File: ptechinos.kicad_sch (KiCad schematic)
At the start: 58 parts, among them J1 Bat_Pos, J2 Battery, J3 Bat_GND, J4 AudioJack4, SW1 SW_Power, SW2 Reset, U1 ProMicro

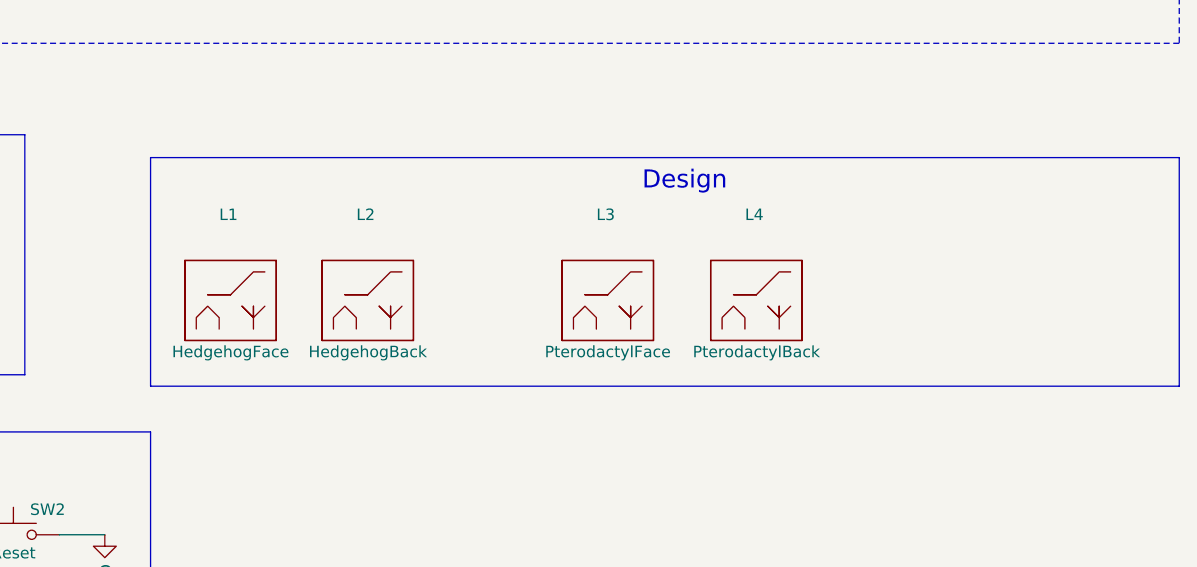
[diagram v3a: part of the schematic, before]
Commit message: ♻️ - Update PCB and schema with new drawing / board name. Update project date to today.
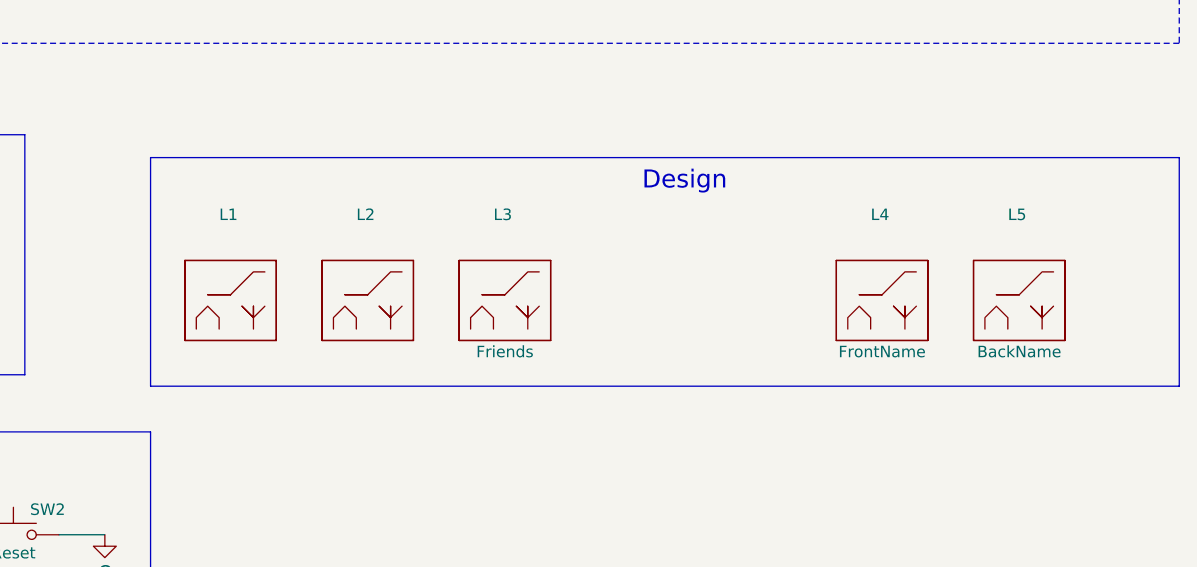
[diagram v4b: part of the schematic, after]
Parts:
- added L5: BackName, ptechinos:Board_name, symbol ptechinos:Logo
- L1: value HedgehogFace -> (none); footprint ptechinos:hedgehog-medium -> (none)
- L2: value HedgehogBack -> (none); footprint ptechinos:hedgehog-medium -> (none)
- L3: value PterodactylFace -> Friends; footprint ptechinos:pterodactyl-medium -> ptechinos:friends-medium
- L4: value PterodactylBack -> FrontName; footprint ptechinos:pterodactyl-medium -> ptechinos:Board_name
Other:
- moved on the sheet: L3
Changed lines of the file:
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@@
   (title_block
     (title "Ptechinos")
-    (date "2022-05-06")
+    (date "2022-05-14")
     (rev "0.4")
     (comment 1 "A crossover between Pteron36 and Balbuzard.")
@@
       (effects (font (size 1.27 1.27)) (justify left))
     )
-    (property "Value" "HedgehogBack" (id 1) (at 189.23 148.59 0))
-    (property "Footprint" "ptechinos:hedgehog-medium" (id 2) (at 189.23 151.13 0)
+    (property "Value" "" (id 1) (at 189.23 148.59 0))
+    (property "Footprint" "" (id 2) (at 189.23 151.13 0)
       (effects (font (size 1.27 1.27)) hide)
     )
@@
     (pin "1")
   )
-  (symbol (lib_id "ptechinos:Logo") (at 232.41 144.78 0) (unit 1)
-    (in_bom yes) (on_board yes)
-    (property "Reference" "L4" (id 0) (at 231.14 133.35 0)
-      (effects (font (size 1.27 1.27)) (justify left))
-    )
-    (property "Value" "PterodactylBack" (id 1) (at 232.41 148.59 0))
-    (property "Footprint" "ptechinos:pterodactyl-medium" (id 2) (at 232.41 151.13 0)
-      (effects (font (size 1.27 1.27)) hide)
-    )
-    (property "Datasheet" "" (id 3) (at 232.41 151.13 0)
-      (effects (font (size 1.27 1.27)) hide)
-    )
-  )
   (symbol (lib_id "Device:D") (at 231.14 83.82 90) (unit 1)
     (in_bom yes) (on_board yes)
@@
     )
     (pin "1")
+  )
+  (symbol (lib_id "ptechinos:Logo") (at 246.38 144.78 0) (unit 1)
+    (in_bom yes) (on_board yes)
+    (property "Reference" "L4" (id 0) (at 245.11 133.35 0)
+      (effects (font (size 1.27 1.27)) (justify left))
+    )
+    (property "Value" "FrontName" (id 1) (at 246.38 148.59 0))
+    (property "Footprint" "ptechinos:Board_name" (id 2) (at 246.38 151.13 0)
+      (effects (font (size 1.27 1.27)) hide)
+    )
+    (property "Datasheet" "" (id 3) (at 246.38 151.13 0)
+      (effects (font (size 1.27 1.27)) hide)
+    )
   )
   (symbol (lib_id "Mechanical:MountingHole") (at 22.86 143.51 0) (unit 1)
@@
     (pin "2")
   )
+  (symbol (lib_id "ptechinos:Logo") (at 261.62 144.78 0) (unit 1)
+    (in_bom yes) (on_board yes)
+    (property "Reference" "L5" (id 0) (at 260.35 133.35 0)
+      (effects (font (size 1.27 1.27)) (justify left))
+    )
+    (property "Value" "BackName" (id 1) (at 261.62 148.59 0))
+    (property "Footprint" "ptechinos:Board_name" (id 2) (at 261.62 151.13 0)
+      (effects (font (size 1.27 1.27)) hide)
+    )
+    (property "Datasheet" "" (id 3) (at 261.62 151.13 0)
+      (effects (font (size 1.27 1.27)) hide)
+    )
+  )
   (symbol (lib_id "Switch:SW_Push") (at 175.26 48.26 0) (unit 1)
     (in_bom yes) (on_board yes)
@@
     (pin "1")
   )
-  (symbol (lib_id "ptechinos:Logo") (at 215.9 144.78 0) (unit 1)
-    (in_bom yes) (on_board yes)
-    (property "Reference" "L3" (id 0) (at 214.63 133.35 0)
-      (effects (font (size 1.27 1.27)) (justify left))
-    )
-    (property "Value" "PterodactylFace" (id 1) (at 215.9 148.59 0))
-    (property "Footprint" "ptechinos:pterodactyl-medium" (id 2) (at 215.9 151.13 0)
-      (effects (font (size 1.27 1.27)) hide)
-    )
-    (property "Datasheet" "" (id 3) (at 215.9 151.13 0)
+  (symbol (lib_id "ptechinos:Logo") (at 204.47 144.78 0) (unit 1)
+    (in_bom yes) (on_board yes)
+    (property "Reference" "L3" (id 0) (at 203.2 133.35 0)
+      (effects (font (size 1.27 1.27)) (justify left))
+    )
+    (property "Value" "Friends" (id 1) (at 204.47 148.59 0))
+    (property "Footprint" "ptechinos:friends-medium" (id 2) (at 204.47 151.13 0)
+      (effects (font (size 1.27 1.27)) hide)
+    )
+    (property "Datasheet" "" (id 3) (at 204.47 151.13 0)
       (effects (font (size 1.27 1.27)) hide)
     )
@@
       (effects (font (size 1.27 1.27)) (justify left))
     )
-    (property "Value" "HedgehogFace" (id 1) (at 173.99 148.59 0))
-    (property "Footprint" "ptechinos:hedgehog-medium" (id 2) (at 173.99 151.13 0)
+    (property "Value" "" (id 1) (at 173.99 148.59 0))
+    (property "Footprint" "" (id 2) (at 173.99 151.13 0)
       (effects (font (size 1.27 1.27)) hide)
     )
@@
     )
     (path "/e2dc4785-3e17-472a-82b9-5050a49344b6"
-      (reference "L1") (unit 1) (value "HedgehogFace") (footprint "ptechinos:hedgehog-medium")
+      (reference "L1") (unit 1) (value "Hedgehog") (footprint "ptechinos:hedgehog-shadow-medium")
     )
     (path "/1b6100b1-6db6-46ed-838f-9445ada9c264"
-      (reference "L2") (unit 1) (value "HedgehogBack") (footprint "ptechinos:hedgehog-medium")
+      (reference "L2") (unit 1) (value "Pterodactyl") (footprint "ptechinos:pterodactyl-shadow-medium")
     )
     (path "/82aa73a4-1fa4-443c-94c3-f62da9681c31"
-      (reference "L3") (unit 1) (value "PterodactylFace") (footprint "ptechinos:pterodactyl-medium")
-    )
-    (path "/2d57ee89-a9fd-4528-970a-f239cc711ad1"
-      (reference "L4") (unit 1) (value "PterodactylBack") (footprint "ptechinos:pterodactyl-medium")
+      (reference "L3") (unit 1) (value "Friends") (footprint "ptechinos:friends-medium")
+    )
+    (path "/4643d211-aeaf-49ae-8bb3-9da5ba42c6e9"
+      (reference "L4") (unit 1) (value "FrontName") (footprint "ptechinos:Board_name")
+    )
+    (path "/5c4fcd53-1fc1-4a33-9f5f-ef92fd04edde"
+      (reference "L5") (unit 1) (value "BackName") (footprint "ptechinos:Board_name")
     )
     (path "/002c56c8-3b30-4e32-9e35-0b9ffbae1671"

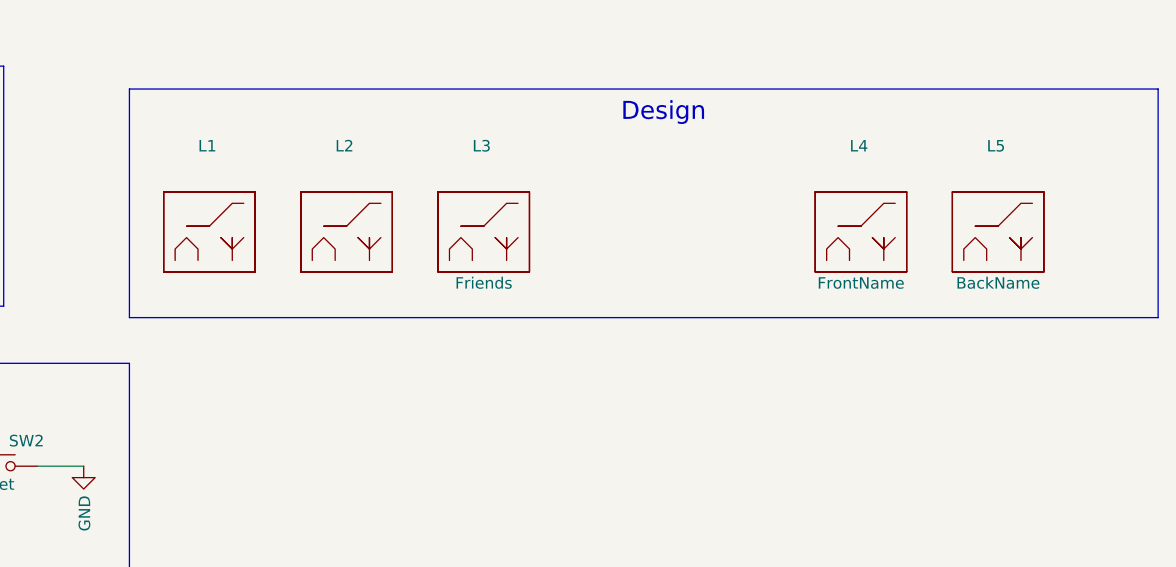
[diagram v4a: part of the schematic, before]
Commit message: 🐛 💄 - Implement drawing / text correction to footprints. See #5388ce217451fca6bf0010363cad309f8bcea6ce. Improve silkscreen graphics position and adjust copper lines to maximize free area.
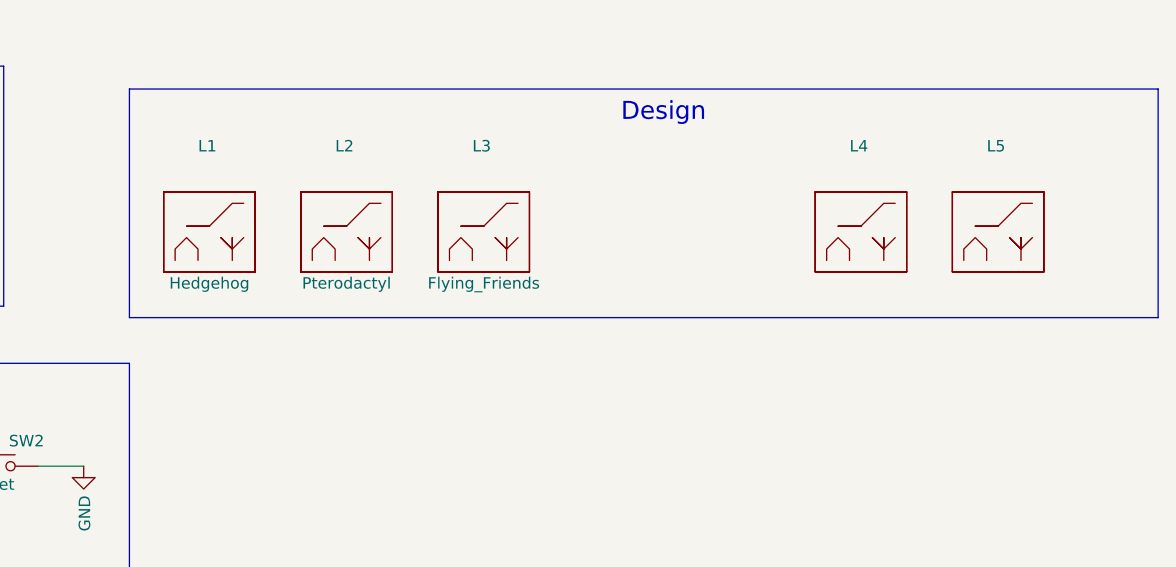
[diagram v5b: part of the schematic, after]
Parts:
- L1: value (none) -> Hedgehog; footprint (none) -> ptechinos:hedgehog-shadow-medium
- L2: value (none) -> Pterodactyl; footprint (none) -> ptechinos:pterodactyl-shadow-medium
- L3: value Friends -> Flying_Friends; footprint ptechinos:friends-medium -> ptechinos:flying-friends-medium
- L4: value FrontName -> (none); footprint ptechinos:Board_name -> (none)
- L5: value BackName -> (none); footprint ptechinos:Board_name -> (none)
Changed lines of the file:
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@@
       (effects (font (size 1.27 1.27)) (justify left))
     )
-    (property "Value" "" (id 1) (at 189.23 148.59 0))
-    (property "Footprint" "" (id 2) (at 189.23 151.13 0)
+    (property "Value" "Pterodactyl" (id 1) (at 189.23 148.59 0))
+    (property "Footprint" "ptechinos:pterodactyl-shadow-medium" (id 2) (at 189.23 151.13 0)
       (effects (font (size 1.27 1.27)) hide)
     )
@@
       (effects (font (size 1.27 1.27)) (justify left))
     )
-    (property "Value" "FrontName" (id 1) (at 246.38 148.59 0))
-    (property "Footprint" "ptechinos:Board_name" (id 2) (at 246.38 151.13 0)
+    (property "Value" "" (id 1) (at 246.38 148.59 0))
+    (property "Footprint" "" (id 2) (at 246.38 151.13 0)
       (effects (font (size 1.27 1.27)) hide)
     )
@@
       (effects (font (size 1.27 1.27)) (justify left))
     )
-    (property "Value" "BackName" (id 1) (at 261.62 148.59 0))
-    (property "Footprint" "ptechinos:Board_name" (id 2) (at 261.62 151.13 0)
+    (property "Value" "" (id 1) (at 261.62 148.59 0))
+    (property "Footprint" "" (id 2) (at 261.62 151.13 0)
       (effects (font (size 1.27 1.27)) hide)
     )
@@
       (effects (font (size 1.27 1.27)) (justify left))
     )
-    (property "Value" "Friends" (id 1) (at 204.47 148.59 0))
-    (property "Footprint" "ptechinos:friends-medium" (id 2) (at 204.47 151.13 0)
+    (property "Value" "Flying_Friends" (id 1) (at 204.47 148.59 0))
+    (property "Footprint" "ptechinos:flying-friends-medium" (id 2) (at 204.47 151.13 0)
       (effects (font (size 1.27 1.27)) hide)
     )
@@
       (effects (font (size 1.27 1.27)) (justify left))
     )
-    (property "Value" "" (id 1) (at 173.99 148.59 0))
-    (property "Footprint" "" (id 2) (at 173.99 151.13 0)
+    (property "Value" "Hedgehog" (id 1) (at 173.99 148.59 0))
+    (property "Footprint" "ptechinos:hedgehog-shadow-medium" (id 2) (at 173.99 151.13 0)
       (effects (font (size 1.27 1.27)) hide)
     )
@@
     )
     (path "/82aa73a4-1fa4-443c-94c3-f62da9681c31"
-      (reference "L3") (unit 1) (value "Friends") (footprint "ptechinos:friends-medium")
+      (reference "L3") (unit 1) (value "Flying_Friends") (footprint "ptechinos:flying-friends-medium")
     )
     (path "/4643d211-aeaf-49ae-8bb3-9da5ba42c6e9"
-      (reference "L4") (unit 1) (value "FrontName") (footprint "ptechinos:Board_name")
+      (reference "L4") (unit 1) (value "FrontName") (footprint "ptechinos:board_name")
     )
     (path "/5c4fcd53-1fc1-4a33-9f5f-ef92fd04edde"
-      (reference "L5") (unit 1) (value "BackName") (footprint "ptechinos:Board_name")
+      (reference "L5") (unit 1) (value "BackName") (footprint "ptechinos:board_name")
     )
     (path "/002c56c8-3b30-4e32-9e35-0b9ffbae1671"

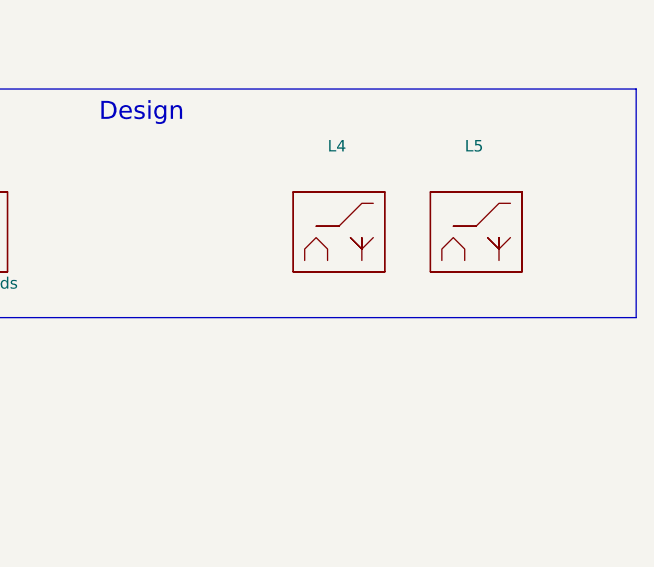
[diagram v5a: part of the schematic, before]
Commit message: ♻️ [Kicad] - Update PCB cutout and plates drawing (bottom/top/keycaps) based on ergogen config. Still required to move switches accordingly.
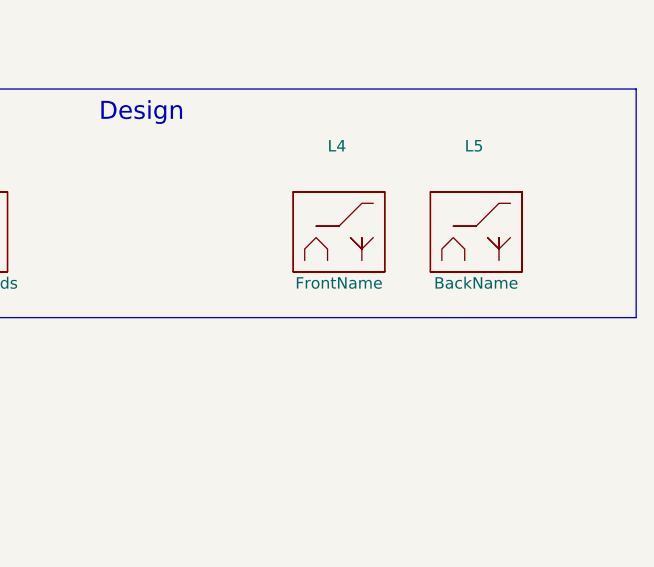
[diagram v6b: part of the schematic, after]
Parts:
- L4: value (none) -> FrontName; footprint (none) -> ptechinos:board_name
- L5: value (none) -> BackName; footprint (none) -> ptechinos:board_name
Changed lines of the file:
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@@
   (title_block
     (title "Ptechinos")
-    (date "2022-05-14")
-    (rev "0.4")
+    (date "2022-05-24")
+    (rev "0.5")
     (comment 1 "A crossover between Pteron36 and Balbuzard.")
   )
@@
       (effects (font (size 1.27 1.27)) (justify left))
     )
-    (property "Value" "" (id 1) (at 246.38 148.59 0))
-    (property "Footprint" "" (id 2) (at 246.38 151.13 0)
+    (property "Value" "FrontName" (id 1) (at 246.38 148.59 0))
+    (property "Footprint" "ptechinos:board_name" (id 2) (at 246.38 151.13 0)
       (effects (font (size 1.27 1.27)) hide)
     )
@@
       (effects (font (size 1.27 1.27)) (justify left))
     )
-    (property "Value" "" (id 1) (at 261.62 148.59 0))
-    (property "Footprint" "" (id 2) (at 261.62 151.13 0)
-      (effects (font (size 1.27 1.27)) hide)
-    )
+    (property "Value" "BackName" (id 1) (at 261.62 148.59 0))
+    (property "Footprint" "ptechinos:board_name" (id 2) (at 261.62 151.13 0)
+      (effects (font (size 1.27 1.27)) hide)
+    )
